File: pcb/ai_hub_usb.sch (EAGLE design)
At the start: 31 parts, among them IC1 FE1.1S

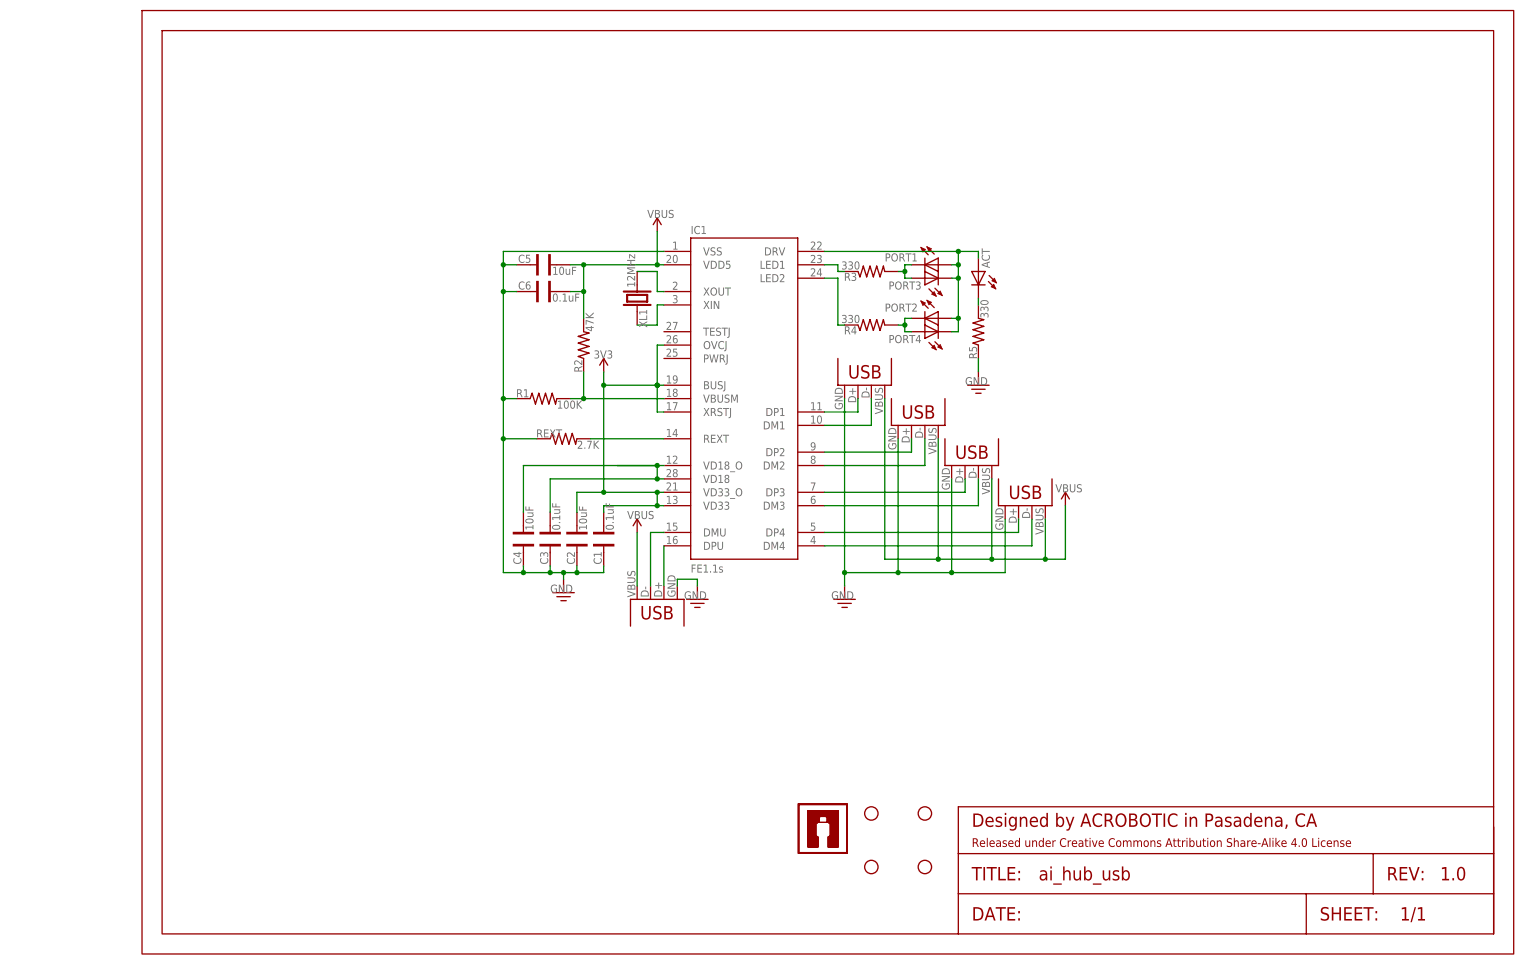
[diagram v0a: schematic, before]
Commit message: redesign: gang power control, smaller layout
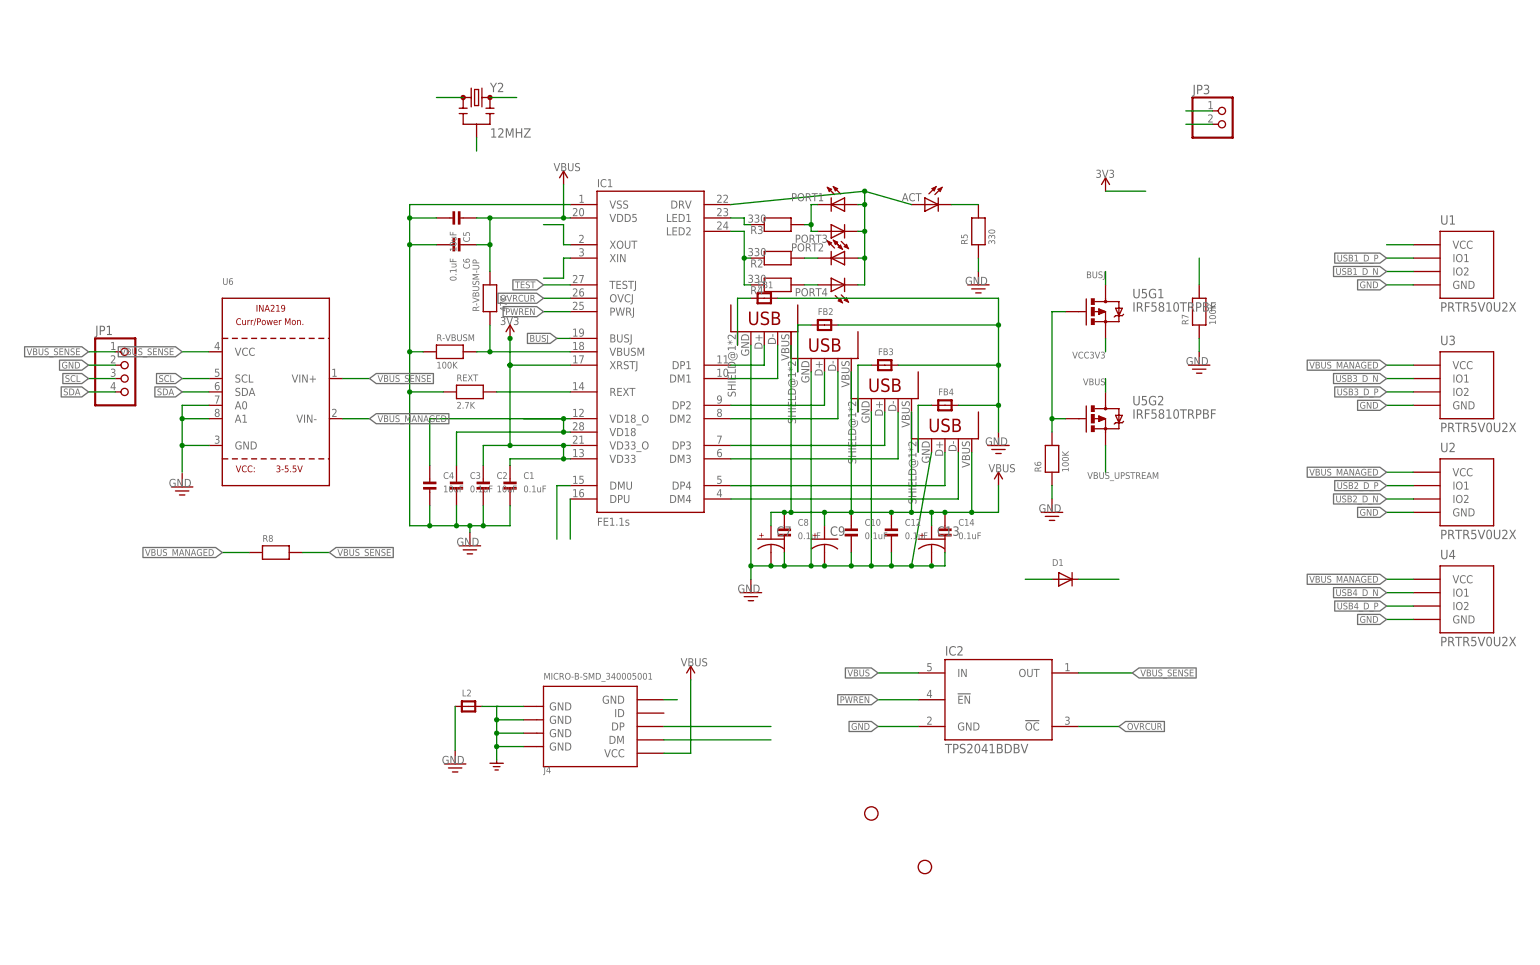
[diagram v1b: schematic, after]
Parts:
- removed FRAME1: FRAME-LETTER, Ai_Miscellany:FRAME-LETTER
- removed R1: 100K, Ai_Passives:RES0603
- removed STANDOFF2, STANDOFF3: STAND-OFF4, Ai_Electromechanical:STAND-OFF4
- removed U$5, U$6: AI-LOGOXS, Ai_Miscellany:AI-LOGOXS
- removed USB5: USBA-PTH, Ai_Connectors:USBA-PTH
- removed XL1: 12MHz, Ai_FrequencyControl:CRYSTALHC49UP
- added C10, C12, C14, C8: 0.1uF, microbuilder:CAP_CERAMIC_0603MP
- added C13, C7, C9: (no value), SparkFun-Passives:CAP_POLD
- added D1: (no value), microbuilder:DIODESMA
- added FB1, FB2, FB3, FB4, L2: (no value), microbuilder:FERRITE_0603MP
- added IC2: TPS2041BDBV, tps204xb_205xb:TPS2041BDBV
- added J4: MICRO-B-SMD_340005001, connectors:USB-MINIUSB-5P-MICRO
- added JP1: (no value), microbuilder:HEADER-1X4ROUND
- added JP3: (no value), microbuilder:HEADER-1X2ROUND
- added R-VBUSM, R6, R7: 100K, microbuilder:RESISTOR_0603MP
- added R-VBUSM-UP: 47K, microbuilder:RESISTOR_0603MP
- added R8: (no value), microbuilder:RESISTOR1206
- added U1, U2, U3, U4: PRTR5V0U2X, esd:PRTR5V0U2X
- added U5: IRF5810TRPBF, SparkFun-DiscreteSemi:MOSFET-PCHANNEL_DUALALT
- added U6: (no value), microbuilder:INA219
- added Y2: 12MHZ, SparkFun-FreqCtrl:RESONATOR16MHZ
- C1, C2, C3, C4, C5, C6: device Ai_Passives:CAP0603 -> microbuilder:CAP_CERAMIC_0603MP
- R2: value 47K -> 330; device Ai_Passives:RES0603 -> microbuilder:RESISTOR_0603MP
- R3, R4, R5, REXT: device Ai_Passives:RES0603 -> microbuilder:RESISTOR_0603MP
- USB1: value USBMICROB-PTH -> USBA-PTH-VERTICAL; device Ai_Connectors:USBMICROB-PTH -> ai_hub_usb:USBA-PTH-VERTICAL
- USB2: device Ai_Connectors:USBA-PTH -> ai_hub_usb:USBA-PTH
- USB3, USB4: value USBA-PTH -> USBA-PTH-VERTICAL; device Ai_Connectors:USBA-PTH -> ai_hub_usb:USBA-PTH-VERTICAL
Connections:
- net N$23 renamed LED1
- net N$25 renamed DRV
- net N$8 renamed VCC1V8
- removed net 3V3: C1.1, C2.1, IC1.BUSJ, IC1.OVCJ, IC1.VD33, IC1.VD33_O, IC1.XRSTJ
- removed net N$11: IC1.DP1, USB5.D+
- removed net N$12: IC1.DM1, USB5.D-
- removed net N$13: IC1.VBUSM, R1.2, R2.1
- removed net N$14: IC1.DP2, USB4.D+
- removed net N$15: IC1.DM2, USB4.D-
- removed net N$16: IC1.DP3, USB3.D+
- removed net N$17: IC1.DM3, USB3.D-
- removed net N$18: IC1.DP4, USB2.D+
- removed net N$19: IC1.DM4, USB2.D-
- removed net N$24: IC1.LED2, R4.1
- removed net N$9: IC1.XIN, XL1.1
- new net BUSJ: IC1.BUSJ, R7.2, U5G1.D
- new net LED2: IC1.LED2, R2.1, R4.1
- new net N$4: FB3.1, USB3.SHIELD
- new net N$5: FB4.1, USB4.SHIELD
- new net OSC_IN: IC1.XIN, Y2.1
- new net OSC_OUT: IC1.XOUT, Y2.3
- new net OVRCUR: IC1.OVCJ, IC2.!OC
- new net PWREN: IC1.PWRJ, IC2.!EN
- new net SCL: JP1.3, U6.SCL
- new net SDA: JP1.4, U6.SDA
- new net TEST: IC1.TESTJ
- new net USB1_D_N: IC1.DM1, U1.IO2, USB1.D-
- new net USB1_D_P: IC1.DP1, U1.IO1, USB1.D+
- new net USB2_D_N: IC1.DM2, U2.IO2, USB2.D-
- new net USB2_D_P: IC1.DP2, U2.IO1, USB2.D+
- new net USB3_D_N: IC1.DM3, U3.IO1, USB3.D-
- new net USB3_D_P: IC1.DP3, U3.IO2, USB3.D+
- new net USB4_D_N: IC1.DM4, U4.IO1, USB4.D-
- new net USB4_D_P: IC1.DP4, U4.IO2, USB4.D+
- new net USB_D_N: IC1.DMU, J4.DM
- new net USB_D_P: IC1.DPU, J4.DP
- new net USB_SHIELD: J4.GND@1, J4.GND@2, J4.GND@3, J4.GND@4, L2.2
- new net VBUS_MANAGED: C10.1, C12.1, C13.+, C14.1, C7.+, C8.1, C9.+, R8.1, U1.VCC, U2.VCC, U3.VCC, U4.VCC, U6.VIN-, USB1.VBUS, USB2.VBUS, USB3.VBUS, USB4.VBUS
- new net VBUS_MONITOR: IC1.VBUSM, R-VBUSM-UP.1, R-VBUSM.2
- new net VBUS_SENSE: IC2.OUT, JP1.1, R8.2, U6.VCC, U6.VIN+
- new net VBUS_UPSTREAM: J4.VCC, U5G2.S
- new net VCC3V3: C1.1, C2.1, IC1.VD33, IC1.VD33_O, IC1.XRSTJ, U5G1.S
- new net VEXT: D1.A, JP3.1, R6.2, U5G1.G, U5G2.G
- net GND: now also C10.2, C12.2, C13.-, C14.2, C7.-, C8.2, C9.-, FB1.2, FB2.2, FB3.2, FB4.2, IC2.GND, J4.GND@5, JP1.2, JP3.2, L2.1, R-VBUSM.1, R6.1, R7.1, U1.GND, U2.GND, U3.GND, U4.GND, U6.A0, U6.A1, U6.GND, Y2.2; no longer R1.1, USB5.GND
- net N$2: now also FB1.1, USB1.SHIELD; no longer IC1.DMU, USB1.D-
- net N$3: now also FB2.1, USB2.SHIELD; no longer IC1.DPU, USB1.D+
- net N$6: now also R2.2; no longer PORT4.A, R4.2
- net N$7: now also PORT4.A, R4.2; no longer IC1.XOUT, XL1.2
- net VBUS: now also D1.C, IC2.IN, R-VBUSM-UP.2, U5G2.D; no longer R2.2, USB1.VBUS, USB2.VBUS, USB3.VBUS, USB4.VBUS, USB5.VBUS
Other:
- moved on the sheet: ACT, C1, C2, C3, C4, C5, C6, IC1, PORT1, PORT2, PORT3, PORT4
